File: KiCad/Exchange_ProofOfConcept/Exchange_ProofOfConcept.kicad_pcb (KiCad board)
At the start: 2 copper layers, 94 x 99.1 mm, 57 parts, among them J1 Connector_PinHeader_2.54mm:Pi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, J2 Conn_01x02, J3 Conn_01x02, J4 Conn_01x02, J5 Connector_PinHeader_2.54mm:Pi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, J6 Connector_PinHeader_2.54mm:Pi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, J7 Screw_Terminal_01x02, J8 Conn_01x03, J9 Screw_Terminal_01x08, U1 MCP23017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

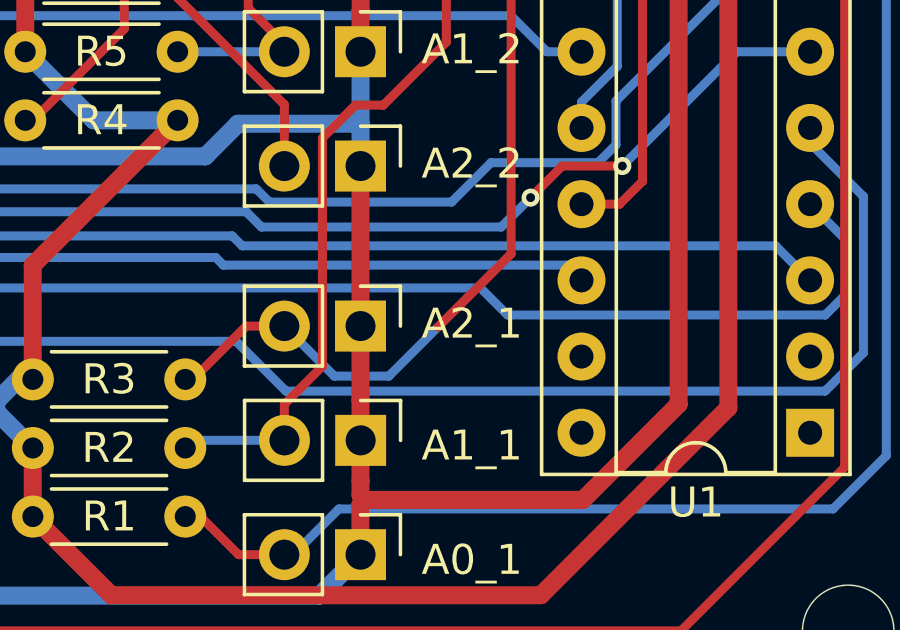
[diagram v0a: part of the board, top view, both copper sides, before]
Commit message: deleted:    KiCad/Exchange_ProofOfConcept/Exchange_ProofOfConcept-backups/Exchange_ProofOfConcept-2024-08-25_222411.zip 	new file:   KiCad/Exchange_ProofOfConcept/Exchange_ProofOfConcept-backups/Exchange_ProofOfConcept-2024-09-09_193050.zip 	modified:   KiCad/Exchange_ProofOfConcept/Exchange_ProofOfConcept.kicad_pcb 	new file:   KiCad/Exchange_ProofOfConcept/~Exchange_ProofOfConcept.kicad_pcb.lck 	deleted:    include/README 	renamed:    src/configurations.h -> include/configurations.h 	new file:   lib/LineStatusHandler/LineStatusHandler.cpp 	new file:   lib/LineStatusHandler/LineStatusHandler.h 	new file:   lib/MT8816/MT8816.cpp 	new file:   lib/MT8816/MT8816.h 	deleted:    lib/README 	renamed:    include/SHK_sense/SHK_sense.cpp -> lib/SHK_sense/SHK_sense.cpp 	renamed:    include/SHK_sense/SHK_sense.h -> lib/SHK_sense/SHK_sense.h 	modified:   src/main.cpp
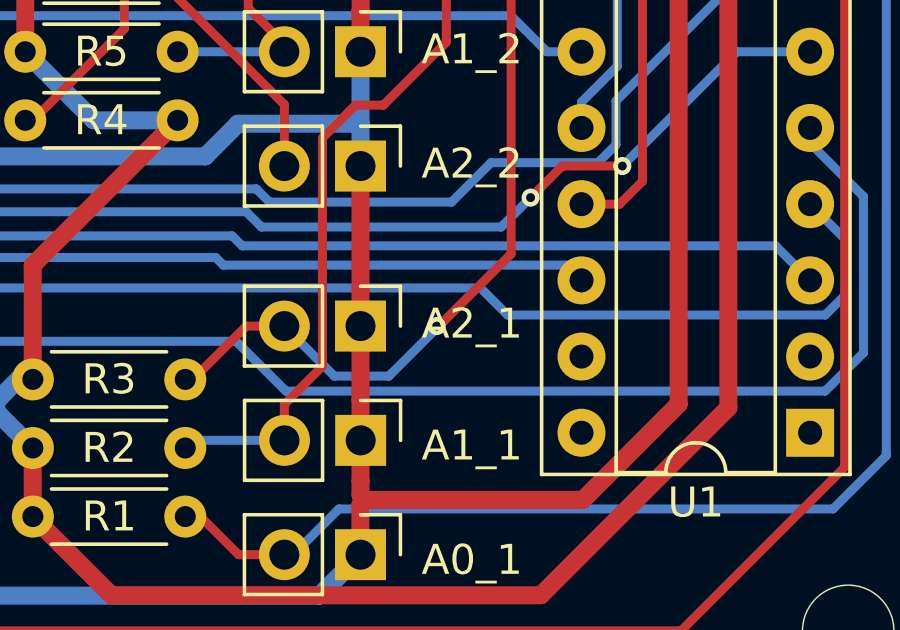
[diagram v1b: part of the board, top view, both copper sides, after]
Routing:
- net Net-(J3-Pin_2): track 44.5 -> 44.6 mm, vias 0 -> 1
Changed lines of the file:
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@@
 	)
 	(segment
-		(start 166.624 109.728)
-		(end 166.624 100.838)
+		(start 164.084 110.236)
+		(end 166.116 110.236)
 		(width 0.3)
 		(layer "F.Cu")
@@
 	)
 	(segment
-		(start 164.084 110.236)
-		(end 166.116 110.236)
+		(start 162.7536 125.8639)
+		(end 162.7536 111.5664)
 		(width 0.3)
 		(layer "F.Cu")
@@
 	)
 	(segment
+		(start 166.116 110.236)
+		(end 166.624 109.728)
+		(width 0.3)
+		(layer "F.Cu")
+		(net 98)
+	)
+	(segment
+		(start 160.274 128.27)
+		(end 160.3475 128.27)
+		(width 0.3)
+		(layer "F.Cu")
+		(net 98)
+	)
+	(segment
 		(start 153.924 128.27)
 		(end 152.146 130.048)
+		(width 0.3)
+		(layer "F.Cu")
+		(net 98)
+	)
+	(segment
+		(start 166.624 100.838)
+		(end 165.1 99.314)
+		(width 0.3)
+		(layer "F.Cu")
+		(net 98)
+	)
+	(segment
+		(start 162.7536 111.5664)
+		(end 164.084 110.236)
 		(width 0.3)
 		(layer "F.Cu")
@@
 	)
 	(segment
-		(start 160.3124 128.3051)
+		(start 166.624 109.728)
+		(end 166.624 100.838)
+		(width 0.3)
+		(layer "F.Cu")
+		(net 98)
+	)
+	(segment
+		(start 160.3475 128.27)
 		(end 162.7536 125.8639)
 		(width 0.3)
@@
 		(net 98)
 	)
-	(segment
-		(start 162.7536 111.5664)
-		(end 164.084 110.236)
-		(width 0.3)
-		(layer "F.Cu")
+	(via
+		(at 160.274 128.27)
+		(size 0.6)
+		(drill 0.3)
+		(layers "F.Cu" "B.Cu")
 		(net 98)
 	)
 	(segment
-		(start 166.624 100.838)
-		(end 165.1 99.314)
+		(start 160.274 128.27)
+		(end 160.274 128.3435)
 		(width 0.3)
-		(layer "F.Cu")
+		(layer "B.Cu")
 		(net 98)
 	)
 	(segment
-		(start 162.7536 125.8639)
-		(end 162.7536 111.5664)
+		(start 158.6795 129.938)
+		(end 156.862 129.938)
 		(width 0.3)
-		(layer "F.Cu")
+		(layer "B.Cu")
 		(net 98)
 	)
 	(segment
-		(start 166.116 110.236)
-		(end 166.624 109.728)
+		(start 160.3475 128.27)
+		(end 160.274 128.27)
 		(width 0.3)
-		(layer "F.Cu")
+		(layer "B.Cu")
 		(net 98)
 	)
@@
 	(segment
 		(start 160.3124 128.3051)
-		(end 158.6795 129.938)
+		(end 160.3475 128.27)
 		(width 0.3)
 		(layer "B.Cu")
@@
 	)
 	(segment
-		(start 158.6795 129.938)
-		(end 156.862 129.938)
+		(start 160.274 128.3435)
+		(end 158.6795 129.938)
 		(width 0.3)
 		(layer "B.Cu")
